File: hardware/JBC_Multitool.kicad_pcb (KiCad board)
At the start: 2 copper layers, 122 x 93 mm, 52 parts, among them J1 Screw_Terminal_01x02, J2 Mini XLR6, J4 Mini XLR6, J5 Mini XLR6, J6 Binder 09-0998-00-05, J7 Binder 09-0998-00-05, K1 RT314005, K10 HF49FD_005-1H12T, K11 HF49FD_005-1H12T, K12 HF49FD_005-1H12T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

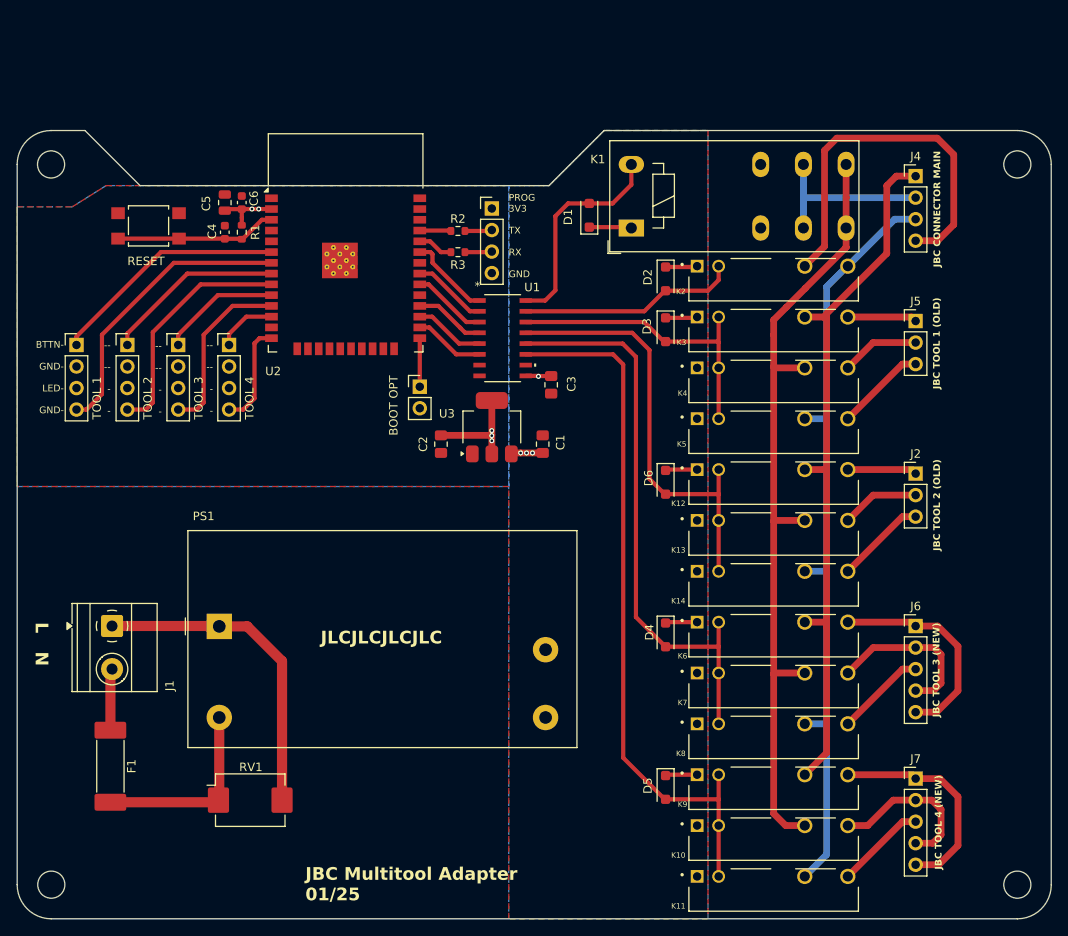
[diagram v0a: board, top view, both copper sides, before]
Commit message: Changes at Silkscreen and Gerber Files
Some cosmetic changes at PCB Silkscreen and namings in Schematic.
Gerber Files updated
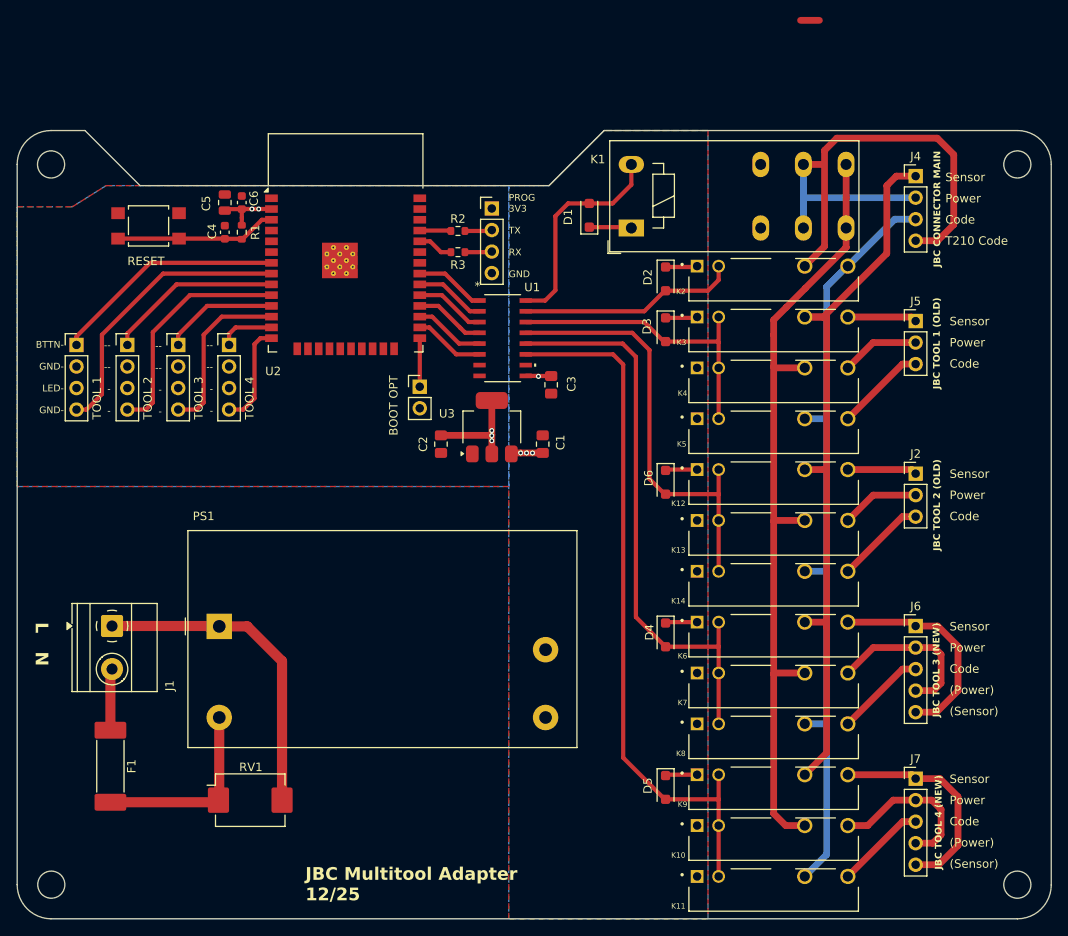
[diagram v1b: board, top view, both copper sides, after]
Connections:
- U2 pad 10: /SELECT_TOOL_3 -> /SELECT_TOOL_LED_2
- U2 pad 11: /SELECT_TOOL_LED_3 -> /SELECT_TOOL_3
- U2 pad 12: /SELECT_TOOL_4 -> /SELECT_TOOL_LED_3
- U2 pad 13: unconnected-(U2-IO14-Pad13) -> /SELECT_TOOL_4
- U2 pad 29: unconnected-(U2-IO5-Pad29) -> /TOOL_1_CTRL
- U2 pad 30: /TOOL_1_CTRL -> /TOOL_SENSOR_CTRL
- U2 pad 31: /TOOL_SENSOR_CTRL -> /TOOL_POWER_CTRL
- U2 pad 33: /TOOL_POWER_CTRL -> unconnected-(U2-IO21-Pad33)
- U2 pad 6: /SELECT_TOOL_1 -> unconnected-(U2-IO34-Pad6)
- U2 pad 7: /SELECT_TOOL_LED_1 -> /SELECT_TOOL_1
- U2 pad 8: /SELECT_TOOL_2 -> /SELECT_TOOL_LED_1
- U2 pad 9: /SELECT_TOOL_LED_2 -> /SELECT_TOOL_2
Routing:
- net /RELAIS_CARD/TOOL_SENSOR: track 85.1 -> 91.8 mm
- net /TOOL_POWER_CTRL: track 10.0 -> 8.37 mm
- net /SELECT_TOOL_LED_1: track 34.3 -> 33.7 mm
- net /TOOL_1_CTRL: track 8.89 -> 8.37 mm
- net /SELECT_TOOL_LED_2: track 28.0 -> 27.5 mm
- net /SELECT_TOOL_3: track 14.1 -> 13.6 mm
- net /TOOL_SENSOR_CTRL: track 8.89 -> 8.37 mm
- net /SELECT_TOOL_LED_3: track 20.8 -> 20.2 mm
- net /SELECT_TOOL_2: track 21.3 -> 20.8 mm
- net /SELECT_TOOL_1: track 28.1 -> 27.6 mm
- net /SELECT_TOOL_4: track 7.14 -> 6.62 mm
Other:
- board text added: "(Power)"
- board text added: "(Sensor)"
- board text added: "Code"
- board text added: "JBC Multitool Adapter 12/25"
- board text added: "Power"
- board text added: "Sensor"
- board text added: "T210 Code"
- board text removed: "JBC Multitool Adapter 01/25"
- board text removed: "JLCJLCJLCJLC"
